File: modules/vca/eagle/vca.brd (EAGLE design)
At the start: 100 x 80 mm, 71 parts, among them IC1 TL074P, IC2 LM13600AN, Q1 2N3906, Q2 2N3906, T1 2N3904, T2 2N3904

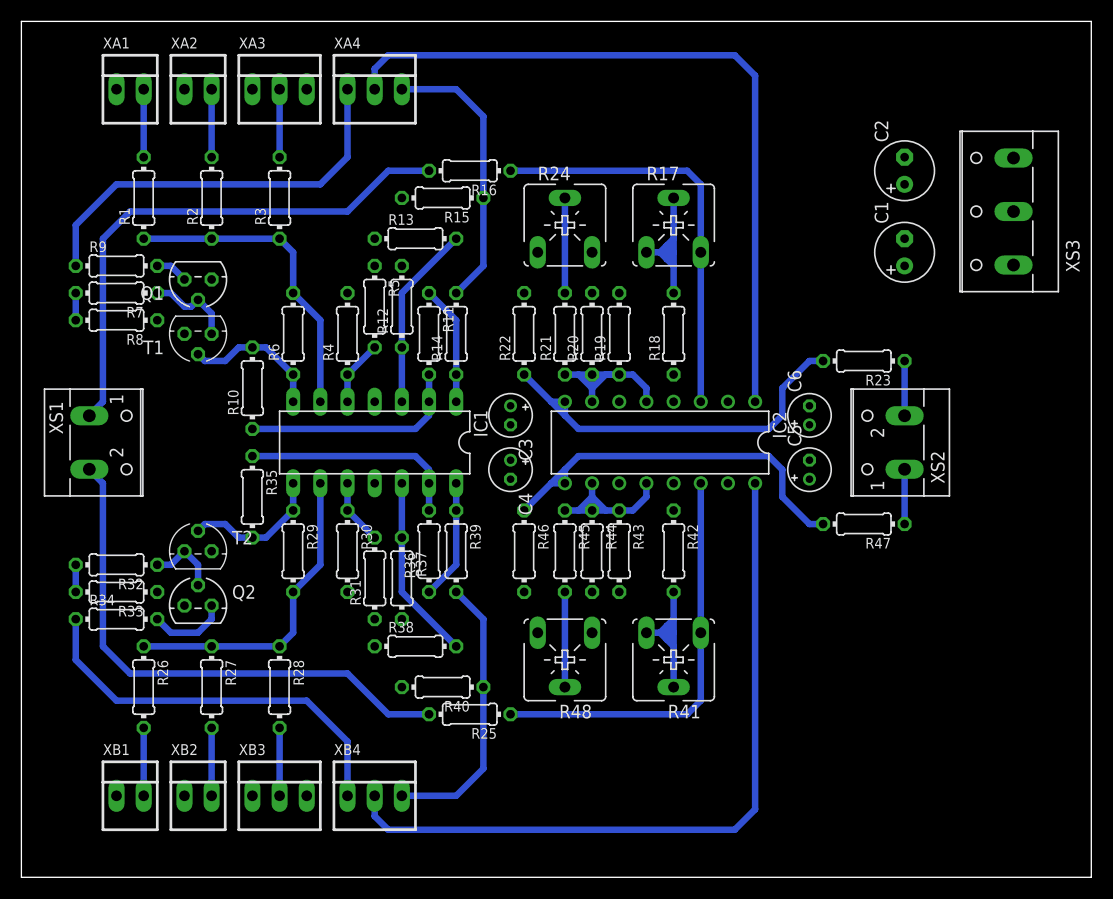
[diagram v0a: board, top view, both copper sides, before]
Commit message: VCA board: drop symmetry in favor of smaller size
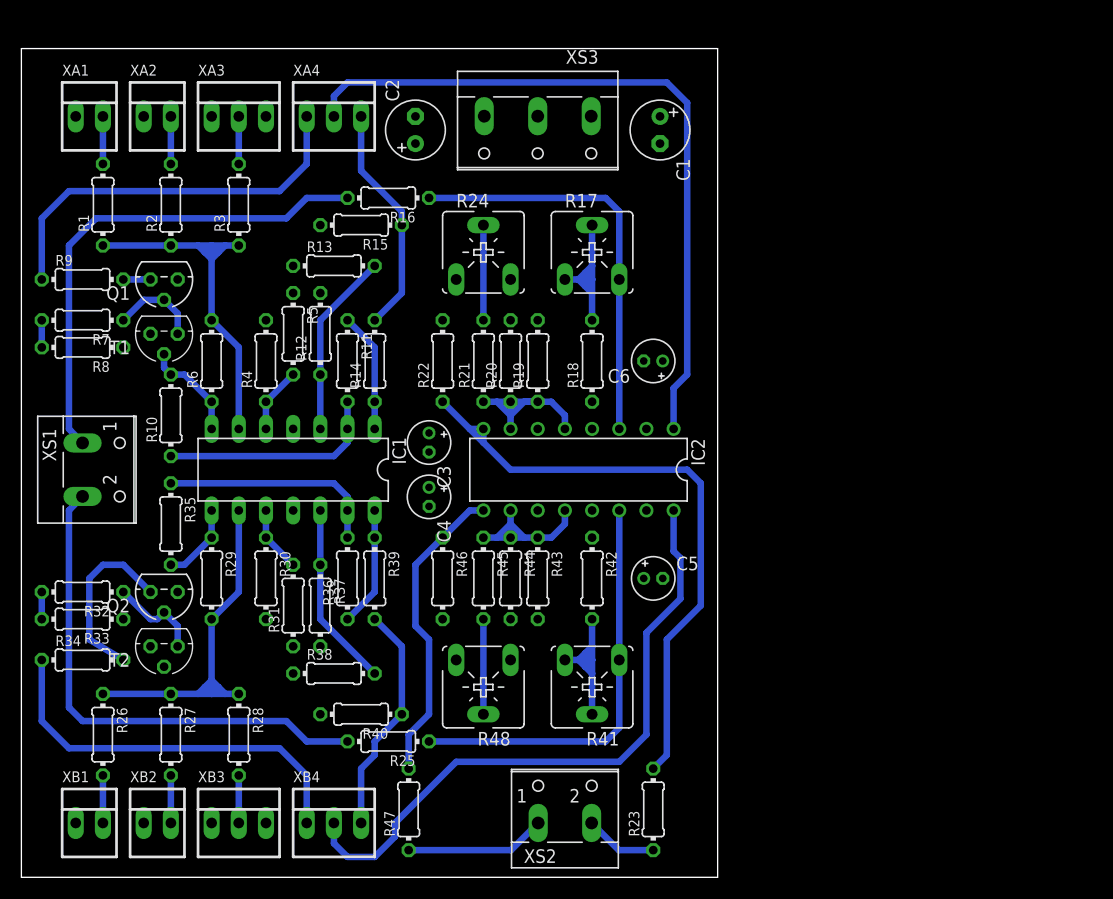
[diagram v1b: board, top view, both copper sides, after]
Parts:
- moved R47 50.2 mm to (36.2, 6.35), turned to 90 degrees
- moved R23 46.3 mm to (59.1, 6.35), turned to 90 degrees
- moved XS2 45.9 mm to (50.8, 6.35), turned to 0 degrees
- moved C2 45.9 mm to (36.8, 69.8)
- moved XS3 43.8 mm to (48.3, 69.8), turned to 180 degrees
- moved C1 25.6 mm to (59.7, 69.8), turned to 270 degrees
- moved C5 17.8 mm to (59.1, 27.9), turned to 0 degrees
- moved C6 15.5 mm to (59.1, 48.3), turned to 180 degrees
- moved T2 9.44 mm to (13.3, 21.6), turned to 180 degrees
- moved R5 8.03 mm to (25.4, 50.8)
- moved R31 8.03 mm to (25.4, 25.4)
- moved IC1 8.03 mm to (25.4, 38.1)
- moved R12 8.03 mm to (27.9, 50.8)
- moved R19 8.03 mm to (48.3, 48.3)
- moved R20 8.03 mm to (45.7, 48.3)
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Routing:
- net N$18: track 36.7 -> 58.3 mm
- net N$32: track 69.3 -> 59.7 mm
- net N$41: track 7.40 -> 16.7 mm
- net N$31: track 5.12 -> 13.2 mm
- net N$49: track 36.7 -> 28.8 mm
- net N$35: track 29.5 -> 36.3 mm
- net N$1: track 29.5 -> 36.3 mm
- net N$36: track 13.3 -> 7.40 mm
- net N$45: track 26.2 -> 21.7 mm
- net N$17: track 26.2 -> 21.7 mm
- net N$7: track 13.3 -> 9.57 mm
- net N$20: track 50.2 -> 46.8 mm
- net N$21: track 50.2 -> 47.6 mm
- net N$39: track 6.77 -> 8.83 mm
- net N$12: track 69.3 -> 67.2 mm
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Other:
- board size 100 x 80 mm -> 65.1 x 77.5 mm

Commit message: Finish dual VCA board design
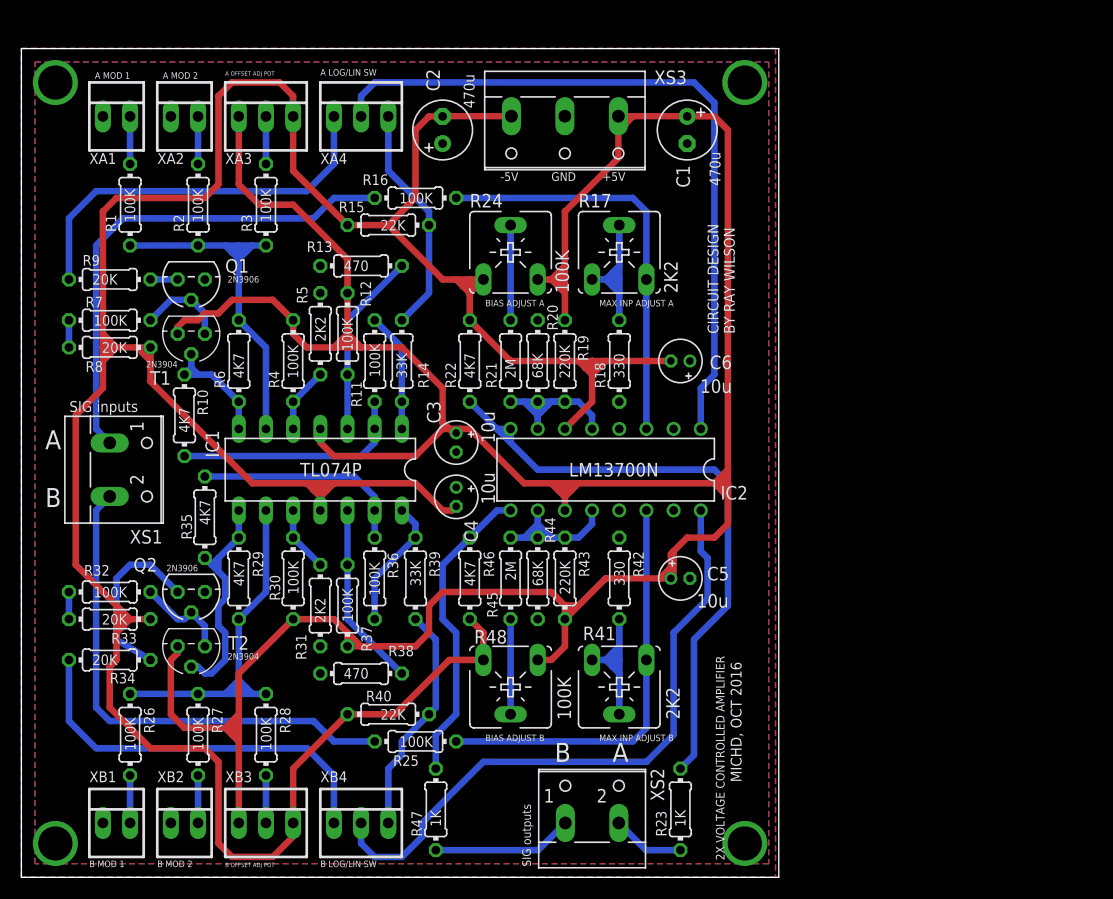
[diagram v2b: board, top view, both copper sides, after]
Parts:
- IC2: value LM13600AN -> LM13700N
- moved R39 3.81 mm to (36.8, 27.9)
- moved R35 3.24 mm to (17.1, 33.7)
- moved XS2 2.54 mm to (53.3, 6.35)
- moved IC1 2.54 mm to (27.9, 38.1)
- moved R11 2.54 mm to (33.0, 48.3)
- moved R31 2.54 mm to (27.9, 25.4)
- moved R36 2.54 mm to (33.0, 27.9)
- moved R5 2.54 mm to (27.9, 50.8)
- moved R2 2.54 mm to (16.5, 62.9)
- moved R27 2.54 mm to (16.5, 13.3)
- moved R32 2.54 mm to (8.26, 26.7)
- moved R33 2.54 mm to (8.26, 24.1)
- moved R34 2.54 mm to (8.26, 20.3)
- moved R7 2.54 mm to (8.26, 52.1)
- moved R8 2.54 mm to (8.26, 49.5)
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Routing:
- net VCC: track 0.00 -> 309.8 mm
- net VEE: track 0.00 -> 294.1 mm
- net N$36: track 7.40 -> 22.2 mm
- net N$19: track 0.00 -> 5.23 mm
- net N$7: track 9.57 -> 11.7 mm
- net N$11: track 20.8 -> 22.1 mm
- net N$43: track 11.2 -> 12.3 mm
- added copper zone on layer 1, net GND
- added copper zone on layer 16, net GND
- added copper zone on layer 1, net N$48
- added copper zone on layer 16, net N$51
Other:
- board size 65.1 x 77.5 mm -> 70.8 x 77.5 mm
- board text added: "+5V"
- board text added: "-5V"
- board text added: "2X VOLTAGE CONTROLLED AMPLIFIER"
- board text added: "A"
- board text added: "B"
- board text added: "BIAS ADJUST A"
- board text added: "BIAS ADJUST B"
- board text added: "CIRCUIT DESIGN BY RAY WILSON"
- board text added: "GND"
- board text added: "MAX INP ADJUST A"
- board text added: "MAX INP ADJUST B"
- board text added: "MICHD, OCT 2016"
